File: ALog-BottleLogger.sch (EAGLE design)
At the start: 103 parts, among them IC2 ATMEGA644M, Q1 220mA/50V/3.5Ω, Q11 220mA/50V/3.5Ω, Q12 4.3A/20V/54mΩ, Q5 4.3A/20V/54mΩ, Q6 4.3A/20V/54mΩ, Q7 4.3A/20V/54mΩ, Q8 220mA/50V/3.5Ω, Q9 220mA/50V/3.5Ω, U2 FT231X-Q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

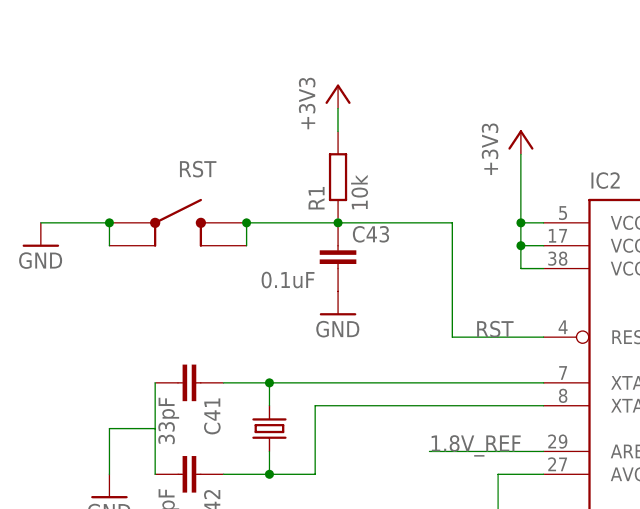
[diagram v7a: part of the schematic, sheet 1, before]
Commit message: Need to fix DTR connection and remove or isolate ground plane under crystal
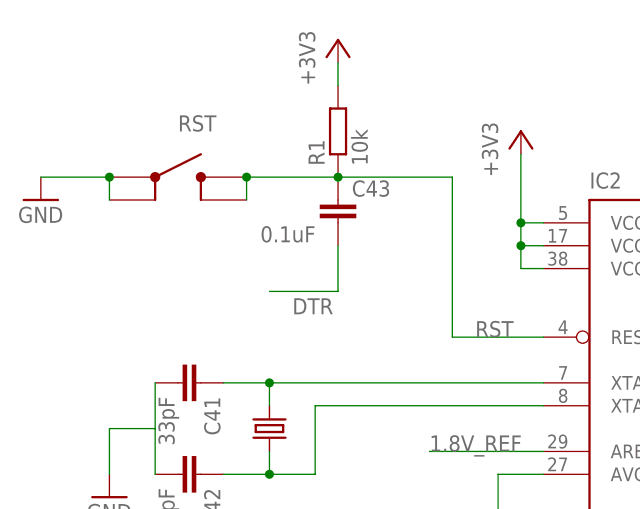
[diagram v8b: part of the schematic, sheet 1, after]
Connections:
- net DTR: now also C43.2
- net GND: no longer C43.2
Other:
- moved on the sheet: C43, R1
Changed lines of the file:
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@@
 <part name="GND50" library="supply1" deviceset="GND" device=""/>
 <part name="C43" library="rcl" deviceset="C-EU" device="C0603" value="0.1uF"/>
-<part name="GND51" library="supply1" deviceset="GND" device=""/>
 <part name="CLOCK_BATT" library="awickert" deviceset="LINX-BAT-HLD-012-SMT-OTL" device="" value="3V Backup Battery"/>
 <part name="D2" library="semicon-smd-ipc" deviceset="DIODE_AC-CA_" device="" value="BAT54C"/>
@@
 <instance part="GND25" gate="1" x="398.78" y="7.62"/>
 <instance part="SD" gate="G$1" x="322.58" y="12.7" rot="R180"/>
-<instance part="R1" gate="G$1" x="165.1" y="58.42" rot="R90"/>
-<instance part="U$4" gate="G$1" x="139.7" y="53.34"/>
+<instance part="R1" gate="G$1" x="165.1" y="63.5" rot="R90"/>
+<instance part="U$4" gate="G$1" x="139.7" y="58.42"/>
 <instance part="GND12" gate="1" x="342.9" y="25.4"/>
 <instance part="GND15" gate="1" x="340.36" y="-10.16"/>
@@
 </instance>
 <instance part="GND49" gate="1" x="182.88" y="-40.64"/>
-<instance part="GND50" gate="1" x="132.08" y="50.8"/>
-<instance part="C43" gate="G$1" x="165.1" y="50.8" smashed="yes">
-<attribute name="NAME" x="166.624" y="51.181" size="1.778" layer="95"/>
-<attribute name="VALUE" x="156.464" y="46.101" size="1.778" layer="96"/>
+<instance part="GND50" gate="1" x="132.08" y="55.88"/>
+<instance part="C43" gate="G$1" x="165.1" y="55.88" smashed="yes">
+<attribute name="NAME" x="166.624" y="56.261" size="1.778" layer="95"/>
+<attribute name="VALUE" x="156.464" y="51.181" size="1.778" layer="96"/>
 </instance>
-<instance part="GND51" gate="1" x="165.1" y="43.18"/>
 <instance part="CLOCK_BATT" gate="G$1" x="414.02" y="-10.16" rot="R90"/>
 <instance part="D2" gate="G$1" x="414.02" y="22.86" rot="R90"/>
@@
 <instance part="+3V1" gate="G$1" x="439.42" y="40.64"/>
 <instance part="+3V2" gate="G$1" x="185.42" y="63.5"/>
-<instance part="+3V3" gate="G$1" x="165.1" y="68.58"/>
+<instance part="+3V3" gate="G$1" x="165.1" y="73.66"/>
 <instance part="L_LPF" gate="G$1" x="167.64" y="5.08"/>
 <instance part="ADECOUP" gate="G$1" x="167.64" y="-12.7"/>
@@
 <segment>
 <pinref part="U$4" gate="G$1" pin="1"/>
-<junction x="139.7" y="53.34"/>
-<wire x1="139.7" y1="53.34" x2="132.08" y2="53.34" width="0.1524" layer="91"/>
-<wire x1="139.7" y1="50.8" x2="139.7" y2="53.34" width="0.1524" layer="91"/>
+<junction x="139.7" y="58.42"/>
+<wire x1="139.7" y1="58.42" x2="132.08" y2="58.42" width="0.1524" layer="91"/>
+<wire x1="139.7" y1="55.88" x2="139.7" y2="58.42" width="0.1524" layer="91"/>
 <pinref part="GND50" gate="1" pin="GND"/>
 <pinref part="U$4" gate="G$1" pin="2"/>
-</segment>
-<segment>
-<pinref part="C43" gate="G$1" pin="2"/>
-<pinref part="GND51" gate="1" pin="GND"/>
 </segment>
 <segment>
@@
 <segment>
 <pinref part="R1" gate="G$1" pin="1"/>
-<wire x1="177.8" y1="53.34" x2="165.1" y2="53.34" width="0.1524" layer="91"/>
-<wire x1="154.94" y1="53.34" x2="165.1" y2="53.34" width="0.1524" layer="91"/>
-<label x="147.32" y="58.42" size="1.778" layer="95"/>
+<wire x1="177.8" y1="58.42" x2="165.1" y2="58.42" width="0.1524" layer="91"/>
+<wire x1="154.94" y1="58.42" x2="165.1" y2="58.42" width="0.1524" layer="91"/>
+<label x="147.32" y="63.5" size="1.778" layer="95"/>
 <pinref part="U$4" gate="G$1" pin="3"/>
-<wire x1="154.94" y1="50.8" x2="154.94" y2="53.34" width="0.1524" layer="91"/>
-<junction x="154.94" y="53.34"/>
+<wire x1="154.94" y1="55.88" x2="154.94" y2="58.42" width="0.1524" layer="91"/>
+<junction x="154.94" y="58.42"/>
 <pinref part="C43" gate="G$1" pin="1"/>
-<junction x="165.1" y="53.34"/>
+<junction x="165.1" y="58.42"/>
 <pinref part="U$4" gate="G$1" pin="4"/>
 <pinref part="IC2" gate="G$1" pin="RESET"/>
 <wire x1="187.96" y1="40.64" x2="177.8" y2="40.64" width="0.1524" layer="91"/>
 <label x="180.34" y="40.64" size="1.778" layer="95"/>
-<wire x1="177.8" y1="40.64" x2="177.8" y2="53.34" width="0.1524" layer="91"/>
+<wire x1="177.8" y1="40.64" x2="177.8" y2="58.42" width="0.1524" layer="91"/>
 </segment>
 </net>
@@
 <segment>
 <pinref part="R1" gate="G$1" pin="2"/>
-<wire x1="165.1" y1="66.04" x2="165.1" y2="63.5" width="0.1524" layer="91"/>
+<wire x1="165.1" y1="71.12" x2="165.1" y2="68.58" width="0.1524" layer="91"/>
 <pinref part="+3V3" gate="G$1" pin="+3V3"/>
 </segment>
@@
 </segment>
 </net>
+<net name="DTR" class="0">
+<segment>
+<pinref part="C43" gate="G$1" pin="2"/>
+<wire x1="165.1" y1="50.8" x2="165.1" y2="45.72" width="0.1524" layer="91"/>
+<wire x1="165.1" y1="45.72" x2="157.48" y2="45.72" width="0.1524" layer="91"/>
+<label x="160.02" y="43.18" size="1.778" layer="95"/>
+</segment>
+</net>
